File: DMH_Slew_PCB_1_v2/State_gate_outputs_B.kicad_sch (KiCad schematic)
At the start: 26 parts, among them J10 TS_Jack_6.35mm_Sw, J61 Conn_01x08_PinHeader, J9 TS_Jack_6.35mm_Sw, Q11 BC548, Q12 BC548, U3 TL074

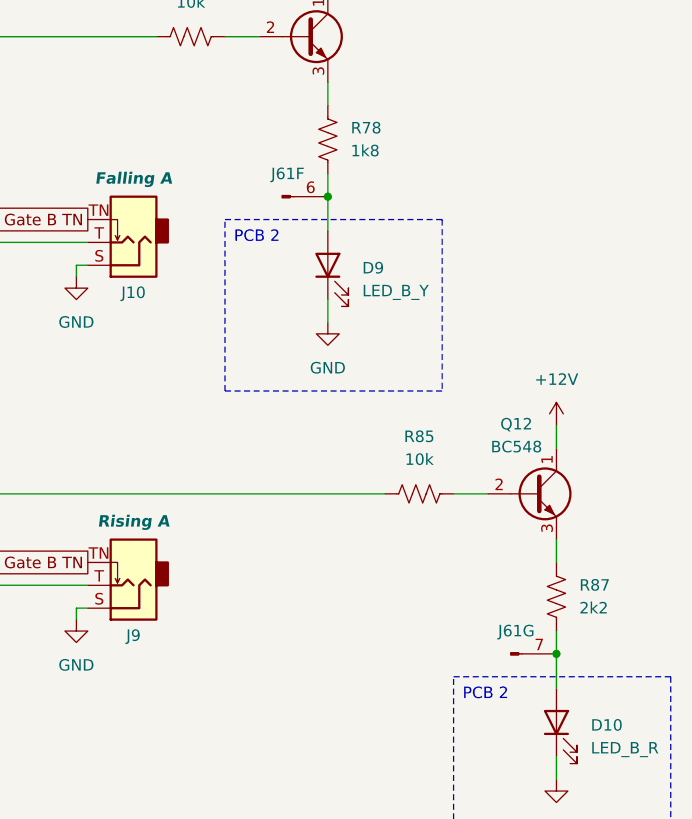
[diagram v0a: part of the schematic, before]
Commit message: PCB 2 component placement done
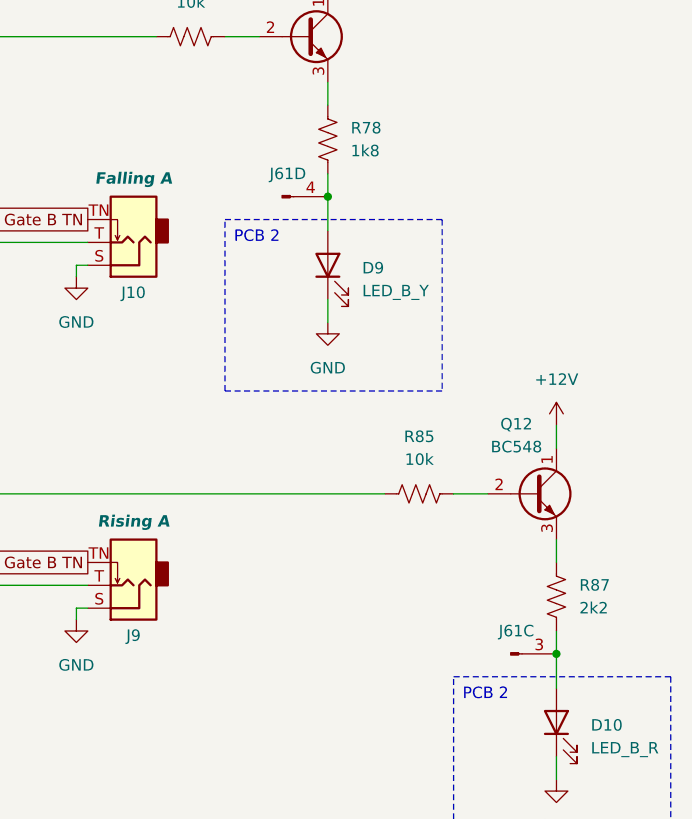
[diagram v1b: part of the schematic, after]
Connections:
- net at D10.2 (A), R87.2: now also J61.3 (Pin_3); no longer J61.7 (Pin_7)
- net at D9.2 (A), R78.2: now also J61.4 (Pin_4); no longer J61.6 (Pin_6)
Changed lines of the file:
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@@
 		(lib_id "SynthStuff:Conn_01x08_PinHeader")
 		(at 251.46 106.68 0)
-		(unit 7)
+		(unit 3)
 		(exclude_from_sim no)
 		(in_bom yes)
@@
 			)
 		)
+		(property "Function" ""
+			(at 251.46 106.68 0)
+			(effects
+				(font
+					(size 1.27 1.27)
+				)
+			)
+		)
 		(pin "3"
 		)
@@
 				(path "/58f4306d-5387-4983-bb08-41a2313fd315/a1b8698d-b4e4-404a-8e9c-ccbb5494e3d6"
 					(reference "J61")
-					(unit 7)
+					(unit 3)
 				)
 			)
@@
 		(lib_id "SynthStuff:Conn_01x08_PinHeader")
 		(at 226.06 55.88 0)
-		(unit 6)
+		(unit 4)
 		(exclude_from_sim no)
 		(in_bom yes)
@@
 			)
 		)
+		(property "Function" ""
+			(at 226.06 55.88 0)
+			(effects
+				(font
+					(size 1.27 1.27)
+				)
+			)
+		)
 		(pin "3"
 		)
@@
 				(path "/58f4306d-5387-4983-bb08-41a2313fd315/a1b8698d-b4e4-404a-8e9c-ccbb5494e3d6"
 					(reference "J61")
-					(unit 6)
-				)
-			)
+					(unit 4)
+				)
+			)

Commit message: PCB 1 component placement ongoing
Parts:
- J10: Function Falling A -> Falling B
- J9: Function Rising A -> Rising B
- Q12: footprint Package_TO_SOT_THT:TO-92_Inline -> Package_TO_SOT_THT:TO-92L_Inline_Wide
- U3: footprint Package_DIP:DIP-16_W7.62mm_Socket -> Package_DIP:DIP-14_W7.62mm_Socket
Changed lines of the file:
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@@
 			)
 		)
-		(property "Function" "Falling A"
+		(property "Function" "Falling B"
 			(at 209.55 53.848 0)
 			(effects
@@
 			)
 		)
-		(property "Function" "Rising A"
+		(property "Function" "Rising B"
 			(at 209.55 91.948 0)
 			(effects
@@
 			)
 		)
-		(property "Footprint" "Package_DIP:DIP-16_W7.62mm_Socket"
+		(property "Footprint" "Package_DIP:DIP-14_W7.62mm_Socket"
 			(at 151.13 101.6 0)
 			(effects
@@
 			)
 		)
-		(property "Footprint" "Package_DIP:DIP-16_W7.62mm_Socket"
+		(property "Footprint" "Package_DIP:DIP-14_W7.62mm_Socket"
 			(at 62.23 78.74 0)
 			(effects
@@
 			)
 		)
-		(property "Footprint" "Package_TO_SOT_THT:TO-92_Inline"
+		(property "Footprint" "Package_TO_SOT_THT:TO-92L_Inline_Wide"
 			(at 259.08 90.805 0)
 			(effects
@@
 			)
 		)
-		(property "Footprint" "Package_DIP:DIP-16_W7.62mm_Socket"
+		(property "Footprint" "Package_DIP:DIP-14_W7.62mm_Socket"
 			(at 151.13 58.42 0)
 			(effects
